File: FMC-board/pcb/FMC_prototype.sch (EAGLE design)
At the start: 111 parts, among them Q1 SSM3J328R, U1 4901, U2 7933, U3 ADN4663, U4 ADN4663, U5 ADN4664, U6 PDS1, U7 4901, U8 FMC_SINGLE_WIDTH_MODULE

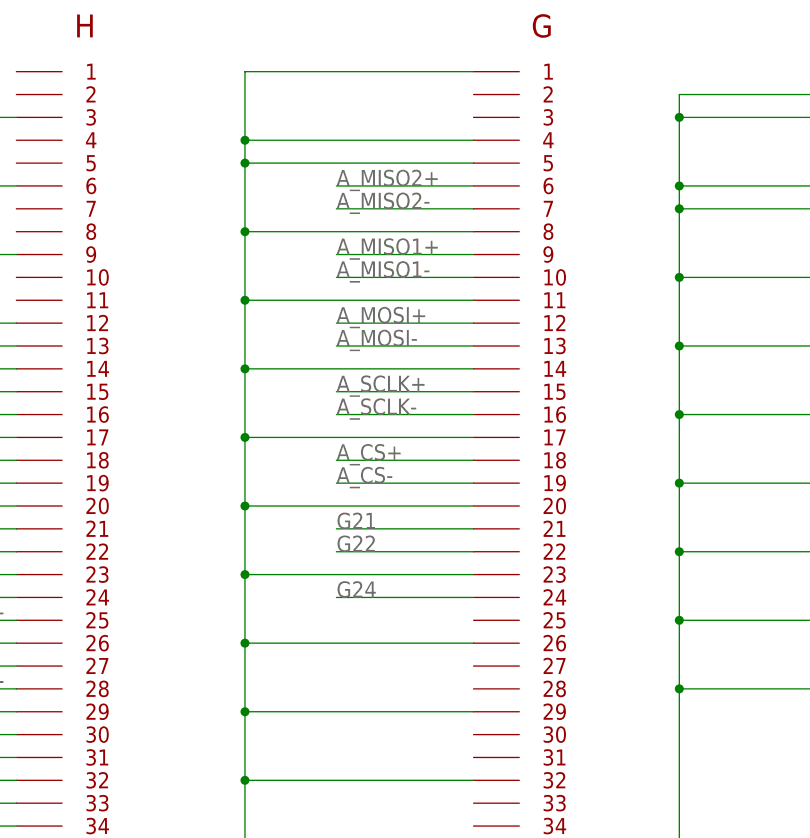
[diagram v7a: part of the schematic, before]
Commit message: Rerouted MISOB so it does not use _CC lines
- CC means clock capable lines and are intented for a different standard
  than LVDS. They should be fine for LVDS signaling, but we had plenty
  of normal LVDS so better safe than sorry
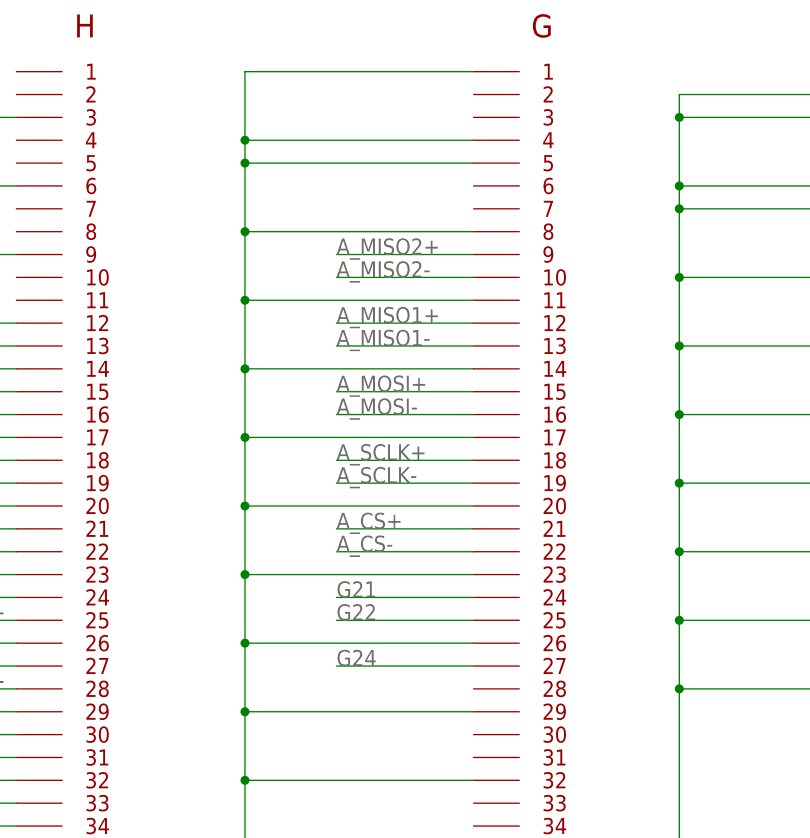
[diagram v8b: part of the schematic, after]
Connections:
- net A_CS+: now also FMCG$1.P$61; no longer FMCG$1.P$58
- net A_CS-: now also FMCG$1.P$62; no longer FMCG$1.P$59
- net A_MISO1+: now also FMCG$1.P$52; no longer FMCG$1.P$49
- net A_MISO1-: now also FMCG$1.P$53; no longer FMCG$1.P$50
- net A_MISO2+: now also FMCG$1.P$49; no longer FMCG$1.P$46
- net A_MISO2-: now also FMCG$1.P$50; no longer FMCG$1.P$47
- net A_MOSI+: now also FMCG$1.P$55; no longer FMCG$1.P$52
- net A_MOSI-: now also FMCG$1.P$56; no longer FMCG$1.P$53
- net A_SCLK+: now also FMCG$1.P$58; no longer FMCG$1.P$55
- net A_SCLK-: now also FMCG$1.P$59; no longer FMCG$1.P$56
- net G21: now also FMCG$1.P$64; no longer FMCG$1.P$61
- net G22: now also FMCG$1.P$65; no longer FMCG$1.P$62
- net G24: now also FMCG$1.P$67; no longer FMCG$1.P$64
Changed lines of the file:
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@@
 </segment>
 <segment>
-<pinref part="FMC" gate="G$1" pin="P$59"/>
-<wire x1="416.56" y1="116.84" x2="401.32" y2="116.84" width="0.1524" layer="91"/>
-<label x="401.32" y="116.84" size="1.778" layer="95"/>
+<label x="401.32" y="109.22" size="1.778" layer="95"/>
+<pinref part="FMC" gate="G$1" pin="P$62"/>
+<wire x1="401.32" y1="109.22" x2="416.56" y2="109.22" width="0.1524" layer="91"/>
 </segment>
 </net>
@@
 </segment>
 <segment>
-<pinref part="FMC" gate="G$1" pin="P$58"/>
-<wire x1="416.56" y1="119.38" x2="401.32" y2="119.38" width="0.1524" layer="91"/>
-<label x="401.32" y="119.38" size="1.778" layer="95"/>
+<label x="401.32" y="111.76" size="1.778" layer="95"/>
+<pinref part="FMC" gate="G$1" pin="P$61"/>
+<wire x1="401.32" y1="111.76" x2="416.56" y2="111.76" width="0.1524" layer="91"/>
 </segment>
 </net>
@@
 </segment>
 <segment>
-<pinref part="FMC" gate="G$1" pin="P$56"/>
-<wire x1="416.56" y1="124.46" x2="401.32" y2="124.46" width="0.1524" layer="91"/>
-<label x="401.32" y="124.46" size="1.778" layer="95"/>
+<label x="401.32" y="116.84" size="1.778" layer="95"/>
+<pinref part="FMC" gate="G$1" pin="P$59"/>
+<wire x1="401.32" y1="116.84" x2="416.56" y2="116.84" width="0.1524" layer="91"/>
 </segment>
 </net>
@@
 </segment>
 <segment>
-<pinref part="FMC" gate="G$1" pin="P$55"/>
-<wire x1="416.56" y1="127" x2="401.32" y2="127" width="0.1524" layer="91"/>
-<label x="401.32" y="127" size="1.778" layer="95"/>
+<label x="401.32" y="119.38" size="1.778" layer="95"/>
+<pinref part="FMC" gate="G$1" pin="P$58"/>
+<wire x1="401.32" y1="119.38" x2="416.56" y2="119.38" width="0.1524" layer="91"/>
 </segment>
 </net>
@@
 </segment>
 <segment>
-<pinref part="FMC" gate="G$1" pin="P$53"/>
-<wire x1="416.56" y1="132.08" x2="401.32" y2="132.08" width="0.1524" layer="91"/>
-<label x="401.32" y="132.08" size="1.778" layer="95"/>
+<label x="401.32" y="124.46" size="1.778" layer="95"/>
+<pinref part="FMC" gate="G$1" pin="P$56"/>
+<wire x1="401.32" y1="124.46" x2="416.56" y2="124.46" width="0.1524" layer="91"/>
 </segment>
 </net>
@@
 </segment>
 <segment>
-<pinref part="FMC" gate="G$1" pin="P$52"/>
-<wire x1="416.56" y1="134.62" x2="401.32" y2="134.62" width="0.1524" layer="91"/>
-<label x="401.32" y="134.62" size="1.778" layer="95"/>
+<label x="401.32" y="127" size="1.778" layer="95"/>
+<pinref part="FMC" gate="G$1" pin="P$55"/>
+<wire x1="401.32" y1="127" x2="416.56" y2="127" width="0.1524" layer="91"/>
 </segment>
 </net>
@@
 </segment>
 <segment>
-<pinref part="FMC" gate="G$1" pin="P$50"/>
-<wire x1="416.56" y1="139.7" x2="401.32" y2="139.7" width="0.1524" layer="91"/>
-<label x="401.32" y="139.7" size="1.778" layer="95"/>
+<label x="401.32" y="132.08" size="1.778" layer="95"/>
+<pinref part="FMC" gate="G$1" pin="P$53"/>
+<wire x1="401.32" y1="132.08" x2="416.56" y2="132.08" width="0.1524" layer="91"/>
 </segment>
 </net>
@@
 </segment>
 <segment>
-<pinref part="FMC" gate="G$1" pin="P$49"/>
-<wire x1="416.56" y1="142.24" x2="401.32" y2="142.24" width="0.1524" layer="91"/>
-<label x="401.32" y="142.24" size="1.778" layer="95"/>
+<label x="401.32" y="134.62" size="1.778" layer="95"/>
+<pinref part="FMC" gate="G$1" pin="P$52"/>
+<wire x1="401.32" y1="134.62" x2="416.56" y2="134.62" width="0.1524" layer="91"/>
 </segment>
 </net>
@@
 </segment>
 <segment>
-<pinref part="FMC" gate="G$1" pin="P$47"/>
-<wire x1="416.56" y1="147.32" x2="401.32" y2="147.32" width="0.1524" layer="91"/>
-<label x="401.32" y="147.32" size="1.778" layer="95"/>
+<label x="401.32" y="139.7" size="1.778" layer="95"/>
+<pinref part="FMC" gate="G$1" pin="P$50"/>
+<wire x1="401.32" y1="139.7" x2="416.56" y2="139.7" width="0.1524" layer="91"/>
 </segment>
 </net>
@@
 </segment>
 <segment>
-<pinref part="FMC" gate="G$1" pin="P$46"/>
-<wire x1="416.56" y1="149.86" x2="401.32" y2="149.86" width="0.1524" layer="91"/>
-<label x="401.32" y="149.86" size="1.778" layer="95"/>
+<label x="401.32" y="142.24" size="1.778" layer="95"/>
+<pinref part="FMC" gate="G$1" pin="P$49"/>
+<wire x1="401.32" y1="142.24" x2="416.56" y2="142.24" width="0.1524" layer="91"/>
 </segment>
 </net>
@@
 <net name="G21" class="0">
 <segment>
-<pinref part="FMC" gate="G$1" pin="P$61"/>
-<wire x1="416.56" y1="111.76" x2="401.32" y2="111.76" width="0.1524" layer="91"/>
-<label x="401.32" y="111.76" size="1.778" layer="95"/>
+<label x="401.32" y="104.14" size="1.778" layer="95"/>
+<pinref part="FMC" gate="G$1" pin="P$64"/>
+<wire x1="401.32" y1="104.14" x2="416.56" y2="104.14" width="0.1524" layer="91"/>
 </segment>
 <segment>
@@
 <net name="G22" class="0">
 <segment>
-<pinref part="FMC" gate="G$1" pin="P$62"/>
-<wire x1="416.56" y1="109.22" x2="401.32" y2="109.22" width="0.1524" layer="91"/>
-<label x="401.32" y="109.22" size="1.778" layer="95"/>
+<label x="401.32" y="101.6" size="1.778" layer="95"/>
+<pinref part="FMC" gate="G$1" pin="P$65"/>
+<wire x1="401.32" y1="101.6" x2="416.56" y2="101.6" width="0.1524" layer="91"/>
 </segment>
 <segment>
@@
 <net name="G24" class="0">
 <segment>
-<pinref part="FMC" gate="G$1" pin="P$64"/>
-<wire x1="416.56" y1="104.14" x2="401.32" y2="104.14" width="0.1524" layer="91"/>
-<label x="401.32" y="104.14" size="1.778" layer="95"/>
-</segment>
-<segment>
+<label x="401.32" y="96.52" size="1.778" layer="95"/>
+<pinref part="FMC" gate="G$1" pin="P$67"/>
+<wire x1="401.32" y1="96.52" x2="416.56" y2="96.52" width="0.1524" layer="91"/>
+</segment>
+<segment>
